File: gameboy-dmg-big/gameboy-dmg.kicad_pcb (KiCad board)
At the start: 2 copper layers, 82.5 x 87.5 mm, 85 parts, among them J1 Conn_01x02, J3 Conn_01x08, J5 Raspberry_Pi_2_3, J6 Conn_01x09, J7 USB_B_Micro, J8 Conn_01x02, P1 RK10J_POT, SW1 SW_DIP_x01, U1 MCP23017_SO, U2 TP4056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

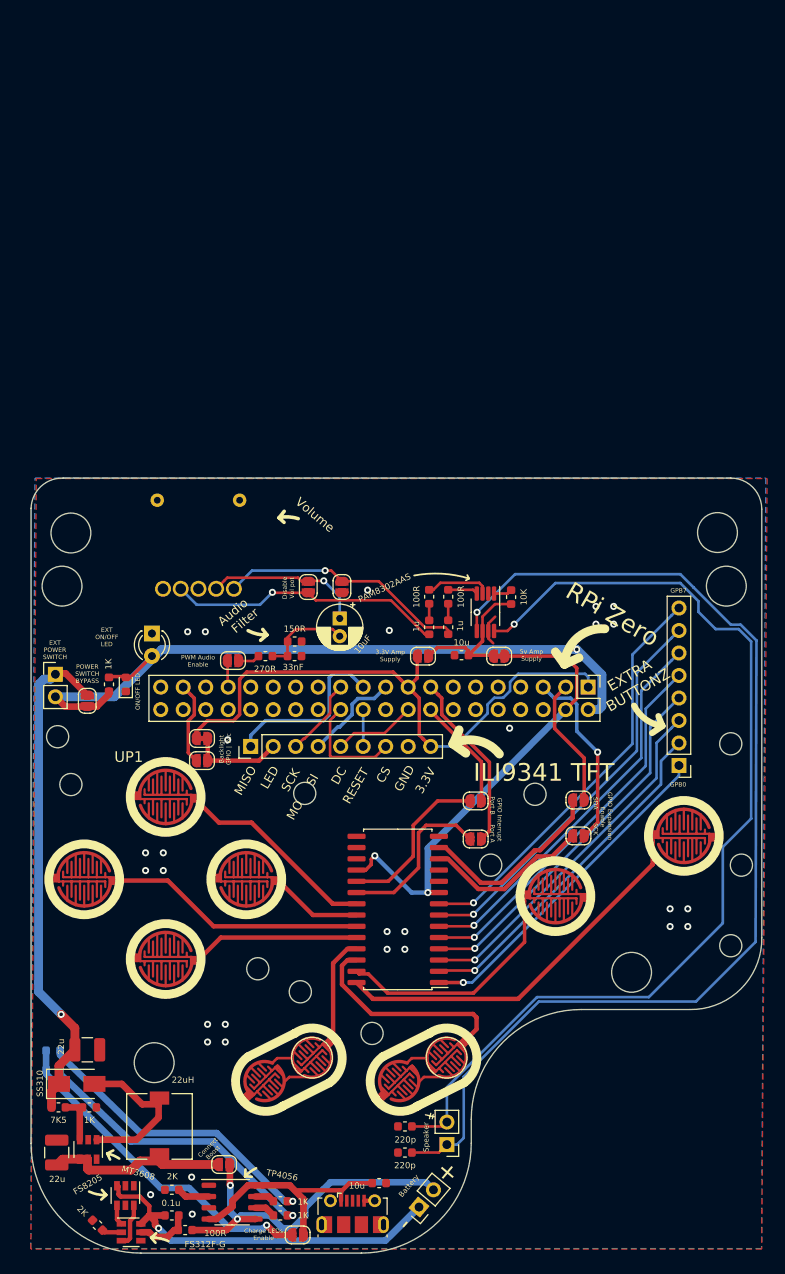
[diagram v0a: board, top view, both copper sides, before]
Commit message: Added ribbon cable TFT to big and routed it
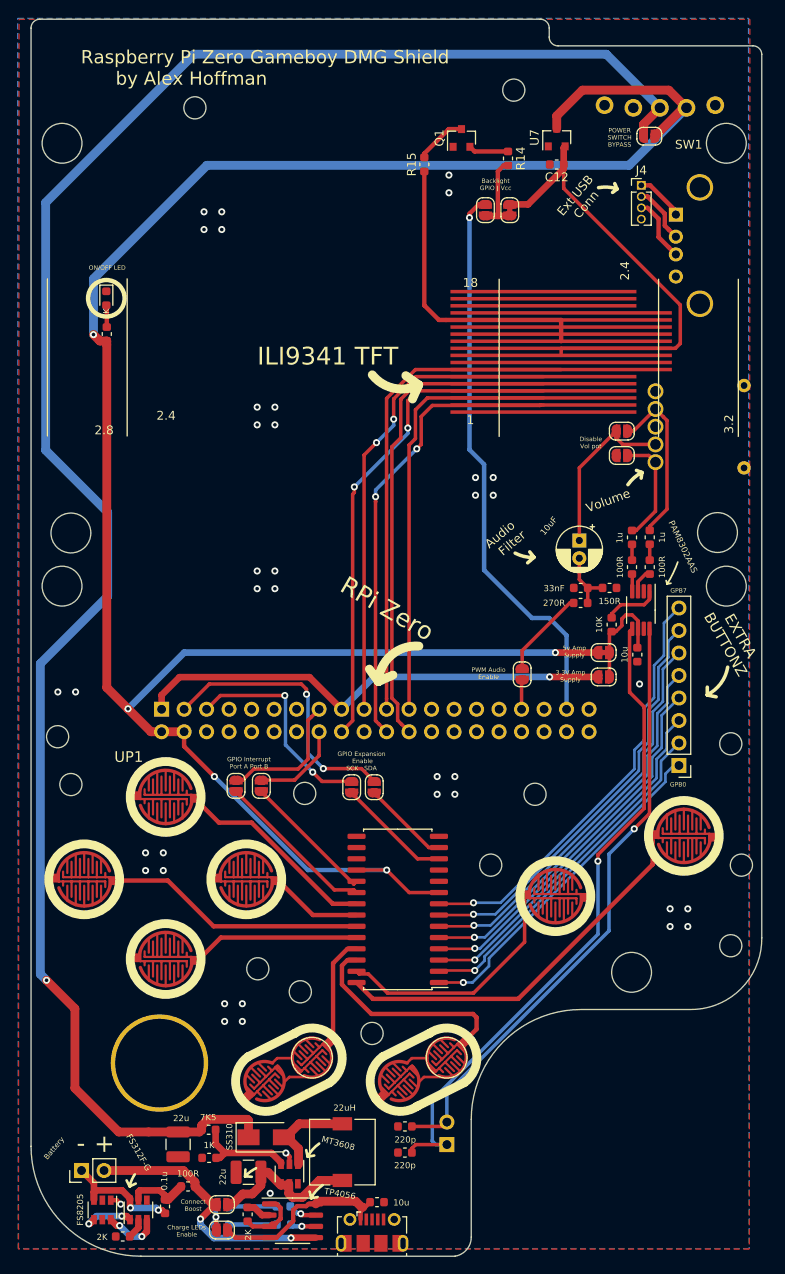
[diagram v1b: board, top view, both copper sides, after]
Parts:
- removed D2: LED, LED_THT:LED_D3.0mm
- removed J6: Conn_01x09, Connector_PinHeader_2.54mm:PinHeader_1x09_P2.54mm_Vertical
- removed the REF** at (84.5, 72.4)
- removed the REF** at (156.5, 72.3)
- removed the REF** at (83.5, 78.4)
- removed the REF** at (157.5, 78.4)
- removed the REF** at (92.9, 130.9)
- added C12: C_Small, Capacitor_SMD:C_0603_1608Metric, F.Cu at (138.3, 29.5)
- added J2: USB_A, Connector_USB:USB_A_Stewart_SS-52100-001_Horizontal, B.Cu at (151.8, 35.1)
- added J4: Conn_01x04, Connector_PinHeader_1.27mm:PinHeader_1x04_P1.27mm_Vertical, F.Cu at (147.9, 31.9)
- added LCD1: MSP_TFT_LCD, pad:MSP_TFT_LCD, F.Cu at (138.8, 57.5)
- added Q1: S8050, Package_TO_SOT_SMD:SOT-23, F.Cu at (127.6, 26.5)
- added R14: 1k, Resistor_SMD:R_0603_1608Metric, F.Cu at (132.8, 28.8)
- added R15: 10R, Resistor_SMD:R_0603_1608Metric, F.Cu at (123.4, 29.5)
- added REF**: MountingHole_2.5mm, MountingHole:MountingHole_2.5mm, F.Cu at (93.5, 130.9)
- added REF**: MountingHole_4.5mm, MountingHole:MountingHole_4.5mm, F.Cu at (82.5, 77.1)
- added REF**: MountingHole_2.5mm, MountingHole:MountingHole_2.5mm, F.Cu at (133.5, 21.1)
- added REF**: MountingHole_2.5mm, MountingHole:MountingHole_2.5mm, F.Cu at (97.5, 23.1)
- added REF**: MountingHole_4.5mm, MountingHole:MountingHole_4.5mm, F.Cu at (157.5, 27.1)
- added REF**: MountingHole_4.5mm, MountingHole:MountingHole_4.5mm, F.Cu at (82.5, 27.1)
- added REF**: MountingHole_4.5mm, MountingHole:MountingHole_4.5mm, F.Cu at (156.5, 71.0)
- added REF**: MountingHole_4.5mm, MountingHole:MountingHole_4.5mm, F.Cu at (157.5, 77.1)
- added REF**: MountingHole_4.5mm, MountingHole:MountingHole_4.5mm, F.Cu at (83.5, 71.1)
- added U7: XC6206PxxxMR, Package_TO_SOT_SMD:SOT-23, F.Cu at (138.3, 26.4)
- J1, J5, R4, R5: moved to B.Cu
- SW1: value SW_DIP_x01 -> SW_DPDT_x2; footprint Connector_PinHeader_2.54mm:PinHeader_1x02_P2.54mm_Vertical -> pad:SS12F23
- moved SW1 95.7 mm to (153.0, 23.1), turned to 180 degrees
- moved G*** 92.4 mm to (92.3, 39.8)
- moved JP8 89.9 mm to (148.8, 26.3), turned to 0 degrees
- moved JP6 69.9 mm to (130.3, 34.6), turned to 270 degrees
- moved JP7 69.0 mm to (133.1, 34.6), turned to 270 degrees
- moved P1 54.7 mm to (149.5, 59.1), turned to 90 degrees
- moved J5 48.2 mm to (93.7, 91.0)
- moved D1 43.7 mm to (87.5, 44.6), turned to 270 degrees
- moved R1 39.6 mm to (87.5, 48.6)
- moved JP10 39.5 mm to (145.7, 59.6), turned to 180 degrees
- moved J8 38.3 mm to (84.7, 143.1), turned to 90 degrees
- moved R2 36.1 mm to (141.1, 79.0)
- moved R3 36.1 mm to (144.3, 77.3)
- moved JP14 34.9 mm to (145.7, 62.4), turned to 180 degrees
- moved G*** 33.3 mm to (98.0, 90.2), turned to 200 degrees
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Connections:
- net /TFT_BACKLIGHT renamed /MSP_LCD/TFT_BACKLIGHT
- JP7 pad 1: +3V3 -> /MSP_LCD/3.3_REG
- SW1 pad 1: /TP4056_LIPO_BOOST/5V_BOOST -> +5V
- SW1 pad 2: +5V -> /TP4056_LIPO_BOOST/5V_BOOST
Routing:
- net /TP4056_LIPO_BOOST/5V_BOOST: track 57.6 -> 214.9 mm
- net +5V: track 132.7 -> 252.3 mm, vias 3 -> 5
- net /TFT_BACKLIGHT_GPIO: track 9.47 -> 63.9 mm, vias 0 -> 1
- net /MSP_LCD/3.3_REG: track 0.00 -> 50.5 mm
- net Net-(C10-Pad1): track 125.3 -> 75.0 mm
- net /TFT_RESET: track 4.16 -> 52.6 mm, vias 0 -> 2
- net /TFT_DC: track 9.34 -> 56.2 mm, vias 0 -> 2
- net Net-(C11-Pad1): track 114.7 -> 69.3 mm
- net /TFT_MOSI: track 11.1 -> 54.4 mm, vias 0 -> 2
- net /TFT_CS: track 12.6 -> 55.6 mm
- net /TFT_SCK: track 8.87 -> 49.1 mm
- net /TFT_MISO: track 20.0 -> 56.2 mm
- net Net-(D3-Pad2): track 38.2 -> 3.58 mm
- net /MSP_LCD/LED-K: track 0.00 -> 33.7 mm
- net /TP4056_LIPO_BOOST/BAT-: track 47.4 -> 14.6 mm, vias 1 -> 2
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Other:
- board size 82.5 x 87.5 mm -> 82.5 x 139.7 mm
- board text added: "Ext USB Conn"
- board text added: "GPIO Expansion Enable SCK SDA"
- board text added: "GPIO Interrupt Port A Port B"
- board text removed: "3.3V"
- board text removed: "CS"
- board text removed: "DC"
- board text removed: "EXT ON/OFF LED"
- board text removed: "EXT POWER SWITCH"
- board text removed: "GND"
- board text removed: "GPIO Expansion Enable SDA SCK"
- board text removed: "GPIO Interrupt Port B Port A"
- board text removed: "LED"
- board text removed: "MISO"
- board text removed: "MO SI"
- board text removed: "RESET"
- board text removed: "SCK"
- board text removed: "TUX"

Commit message: Shifter RPi up
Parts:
- moved G*** 74.6 mm to (145.5, 92.0)
- moved J5 25.9 mm to (94.5, 65.2)
- moved G*** 11.6 mm to (102.6, 100.8)
- moved JP1 8.85 mm to (134.7, 78.2), turned to 270 degrees
- moved JP12 3.00 mm to (143.8, 84.3)
- moved JP13 2.35 mm to (143.8, 87.0)
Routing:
- net +3V3: track 54.7 -> 98.0 mm
- net /TFT_CS: track 55.6 -> 27.2 mm, vias 0 -> 1
- net /TFT_RESET: track 52.6 -> 24.2 mm, vias 2 -> 0
- net /TFT_DC: track 56.2 -> 28.3 mm, vias 2 -> 0
- net /TFT_MOSI: track 54.4 -> 26.7 mm, vias 2 -> 1
- net /TFT_MISO: track 56.2 -> 28.5 mm, vias 0 -> 1
- net /TFT_SCK: track 49.1 -> 21.7 mm, vias 0 -> 1
- net /TFT_BACKLIGHT_GPIO: track 63.9 -> 37.4 mm
- net /GPIO_INTB_PI: track 10.4 -> 34.3 mm
- net /GPIO_INTA_PI: track 15.3 -> 38.0 mm
- net +5V: track 252.3 -> 235.6 mm, vias 5 -> 3
- net /GPIO_SCK_PI: track 24.3 -> 40.5 mm
- net /GPIO_SDA_PI: track 31.3 -> 43.1 mm
- net Net-(J5-Pad33): track 3.33 -> 13.3 mm
- net /PWM_AUDIO_OUT: track 10.1 -> 5.62 mm
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
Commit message: Fixed up big board
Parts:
- moved JP2 20.2 mm to (127.9, 84.0)
- moved JP4 19.2 mm to (116.3, 84.2)
- moved JP5 19.2 mm to (113.5, 84.2)
- moved JP3 17.4 mm to (125.2, 84.0)
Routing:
- net +3V3: track 98.0 -> 64.7 mm, vias 1 -> 0
- net /GPIO_INTA_PI: track 38.0 -> 19.9 mm
- net /GPIO_INTB_PI: track 34.3 -> 18.0 mm
- net /GPIO_INTA: track 18.3 -> 34.1 mm
- net /GPIO_SDA: track 9.85 -> 23.8 mm
- net /GPIO_SCK: track 12.9 -> 26.8 mm
- net /GPIO_INTB: track 15.4 -> 29.1 mm
- net +5V: track 235.6 -> 223.4 mm
- net /GPIO_SDA_PI: track 43.1 -> 36.8 mm
- net /GPIO_SCK_PI: track 40.5 -> 37.0 mm
- net GND: vias 37 -> 41
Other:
- board text added: "GPIO Expansion Enable SDA SCK"
- board text removed: "GPIO Expansion Enable SCK SDA"

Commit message: Big board gerbers
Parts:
- C12: value C_Small -> 100n
- moved J8 0.85 mm to (83.8, 143.1)
- moved C3 0.85 mm to (93.3, 147.1)
- moved R8 0.85 mm to (88.5, 150.5)
- moved U3 0.85 mm to (90.3, 147.5)
- moved U4 0.85 mm to (86.2, 147.5)
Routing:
- net /TP4056_LIPO_BOOST/5V_BOOST: track 214.9 -> 232.0 mm
- net Net-(C3-Pad1): track 7.10 -> 7.93 mm
- net GND: vias 41 -> 43
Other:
- outline, holes or cut-outs redrawn
- board text added: "Backlight GPIO| Vcc"
- board text added: "Charge LEDs"
- board text removed: "Backlight GPIO | Vcc"
- board text removed: "Charge LEDs Enable"

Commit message: Little board gerbers
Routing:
- net (no net): track 5.85 -> 0.75 mm
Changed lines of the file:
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@@
     (thickness 1.6)
     (drawings 77)
-    (tracks 587)
+    (tracks 590)
     (zones 0)
     (modules 95)
@@
   )
   (setup
-    (last_trace_width 0.3)
+    (last_trace_width 0.5)
     (user_trace_width 0.3)
     (user_trace_width 0.4)
@@
     (add_net "Net-(U6-Pad2)")
   )
+  (module MountingHole:MountingHole_2.5mm (layer F.Cu)
+    (at 93.5 130.95)
+    (descr "Mounting Hole 2.5mm, no annular")
+    (tags "mounting hole 2.5mm no annular")
+    (attr virtual)
+    (fp_text reference REF** (at 0 -3.5) (layer F.SilkS) hide
+      (effects (font (size 0.8 0.8) (thickness 0.15)))
+    )
+    (fp_text value MountingHole_2.5mm (at 0 3.5) (layer F.SilkS) hide
+      (effects (font (size 0.7 0.7) (thickness 0.12)))
+    )
+    (fp_text user %R (at 0.3 0) (layer F.SilkS) hide
+      (effects (font (size 0.8 0.8) (thickness 0.15)))
+    )
+    (fp_circle (center 0 0) (end 2.5 0) (layer Cmts.User) (width 0.15))
+    (fp_circle (center 0 0) (end 2.75 0) (layer F.CrtYd) (width 0.05))
+    (pad "" np_thru_hole circle (at 0 0) (size 10 10) (drill 10) (layers *.Cu *.Mask))
+  )
   (module pad:Tux (layer B.Cu)
     (at 102.6 100.85 200)
@@
     )
   )
-  (module MountingHole:MountingHole_2.5mm (layer F.Cu)
-    (at 93.5 130.95)
-    (descr "Mounting Hole 2.5mm, no annular")
-    (tags "mounting hole 2.5mm no annular")
-    (attr virtual)
-    (fp_text reference REF** (at 0 -3.5) (layer F.SilkS) hide
-      (effects (font (size 0.8 0.8) (thickness 0.15)))
-    )
-    (fp_text value MountingHole_2.5mm (at 0 3.5) (layer F.SilkS) hide
-      (effects (font (size 0.7 0.7) (thickness 0.12)))
-    )
-    (fp_text user %R (at 0.3 0) (layer F.SilkS) hide
-      (effects (font (size 0.8 0.8) (thickness 0.15)))
-    )
-    (fp_circle (center 0 0) (end 2.5 0) (layer Cmts.User) (width 0.15))
-    (fp_circle (center 0 0) (end 2.75 0) (layer F.CrtYd) (width 0.05))
-    (pad "" np_thru_hole circle (at 0 0) (size 10 10) (drill 10) (layers *.Cu *.Mask))
-  )
   (module Connector_PinHeader_2.54mm:PinHeader_2x20_P2.54mm_Vertical (layer B.Cu)
     (at 94.5 65.15 270)
@@
   (gr_line (start 161.5 17.080241) (end 161.5 116.8) (layer Edge.Cuts) (width 0.05))
   (segment (start 135.65 101.2) (end 135.65 100.452408) (width 0.4) (layer F.Cu) (net 0))
-  (segment (start 93.4 135.6) (end 91.55 135.6) (width 0.75) (layer F.Cu) (net 0))
-  (segment (start 91.55 135.6) (end 89.25 133.3) (width 0.75) (layer F.Cu) (net 0))
   (segment (start 140.9 76.35) (end 141.85 77.3) (width 0.4) (layer F.Cu) (net 1))
   (segment (start 140.9 73.95) (end 140.9 76.35) (width 0.4) (layer F.Cu) (net 1))
@@
   (segment (start 117.59501 123.70001) (end 133.99999 123.70001) (width 0.5) (layer F.Cu) (net 6))
   (segment (start 115.75 121.855) (end 117.59501 123.70001) (width 0.5) (layer F.Cu) (net 6))
-  (segment (start 149.180935 105.881903) (end 149.110839 105.626049) (width 0.5) (layer F.Cu) (net 6))
-  (segment (start 133.99999 123.70001) (end 149.180935 108.519065) (width 0.5) (layer F.Cu) (net 6))
-  (segment (start 149.180935 108.519065) (end 149.180935 105.881903) (width 0.5) (layer F.Cu) (net 6))
+  (segment (start 149.04 105.47) (end 149.046001 105.144217) (width 0.5) (layer F.Cu) (net 6))
+  (segment (start 148.0375 106.4725) (end 149.04 105.47) (width 0.5) (layer F.Cu) (net 6))
+  (segment (start 148.0375 109.6625) (end 148.0375 106.4725) (width 0.5) (layer F.Cu) (net 6))
+  (segment (start 133.99999 123.70001) (end 148.0375 109.6625) (width 0.5) (layer F.Cu) (net 6))
   (segment (start 117.085 120.885) (end 119.25 123.05) (width 0.4) (layer F.Cu) (net 7))
   (segment (start 115.75 120.585) (end 116.05 120.885) (width 0.4) (layer F.Cu) (net 7))
@@
   (segment (start 140.1125 78.85) (end 140.2625 79) (width 0.4) (layer F.Cu) (net 80))
   (segment (start 134.7 78.85) (end 140.1125 78.85) (width 0.4) (layer F.Cu) (net 80))
-  (segment (start 147 59.6) (end 149.5 57.1) (width 0.4) (layer F.Cu) (net 81))
-  (segment (start 146.35 59.6) (end 147 59.6) (width 0.4) (layer F.Cu) (net 81))
   (segment (start 150.399999 57.999999) (end 149.5 57.1) (width 0.4) (layer F.Cu) (net 81))
   (segment (start 150.800001 58.400001) (end 150.399999 57.999999) (width 0.4) (layer F.Cu) (net 81))
@@
   (segment (start 148.85 70.3625) (end 150.800001 68.412499) (width 0.4) (layer F.Cu) (net 81))
   (segment (start 148.85 70.8) (end 148.85 70.3625) (width 0.4) (layer F.Cu) (net 81))
+  (segment (start 147 59.6) (end 149.5 57.1) (width 0.3) (layer F.Cu) (net 81))
+  (segment (start 146.35 59.6) (end 147 59.6) (width 0.3) (layer F.Cu) (net 81))
   (segment (start 148.85 72.375) (end 148.85 74.1625) (width 0.4) (layer F.Cu) (net 82))
   (segment (start 146.85 72.3875) (end 146.85 74.1625) (width 0.4) (layer F.Cu) (net 83))
@@
   (segment (start 145.575 79.2) (end 148.217478 79.2) (width 0.4) (layer F.Cu) (net 89))
   (segment (start 148.217478 79.2) (end 148.825 78.592478) (width 0.4) (layer F.Cu) (net 89))
-  (segment (start 145.05 60.347592) (end 145.05 59.6) (width 0.4) (layer F.Cu) (net 91))
-  (segment (start 145.802408 61.1) (end 145.05 60.347592) (width 0.4) (layer F.Cu) (net 91))
-  (segment (start 149.5 61.1) (end 145.802408 61.1) (width 0.4) (layer F.Cu) (net 91))
-  (segment (start 140.9 63.75) (end 145.05 59.6) (width 0.4) (layer F.Cu) (net 91))
-  (segment (start 140.9 71.95) (end 140.9 63.75) (width 0.4) (layer F.Cu) (net 91))
+  (segment (start 141.559999 63.090001) (end 144.595936 60.054064) (width 0.3) (layer F.Cu) (net 91))
+  (segment (start 141.559999 70.190001) (end 141.559999 63.090001) (width 0.3) (layer F.Cu) (net 91))
+  (segment (start 140.9 70.85) (end 141.559999 70.190001) (width 0.3) (layer F.Cu) (net 91))
+  (segment (start 144.595936 60.054064) (end 145.05 59.6) (width 0.3) (layer F.Cu) (net 91))
+  (segment (start 140.9 71.95) (end 140.9 70.85) (width 0.3) (layer F.Cu) (net 91))
+  (segment (start 145.802408 61.1) (end 148.227208 61.1) (width 0.3) (layer F.Cu) (net 91))
+  (segment (start 145.05 60.347592) (end 145.802408 61.1) (width 0.3) (layer F.Cu) (net 91))
+  (segment (start 148.227208 61.1) (end 149.5 61.1) (width 0.3) (layer F.Cu) (net 91))
+  (segment (start 145.05 59.6) (end 145.05 60.347592) (width 0.3) (layer F.Cu) (net 91))
   (segment (start 148.75 62.35) (end 149.5 63.1) (width 0.4) (layer F.Cu) (net 92))
   (segment (start 146.35 62.35) (end 148.75 62.35) (width 0.4) (layer F.Cu) (net 92))
